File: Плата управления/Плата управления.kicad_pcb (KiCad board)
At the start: 6 copper layers, 67 x 68.5 mm, 114 parts, among them J1 Conn_02x10_Odd_Even, J10 Conn_02x03_Odd_Even, J2 CAN2, J3 CAN1, J4 A, J5 B, J6 C, J7 RS485, J8 Conn_02x03_Odd_Even, J9 Conn_01x06, U1 AT25xxx, U2 LMV7239M5, U3 LMV321, U4 STM32F767VITx, U5 INA283, U6 ADM3491ExR, U7 ASEMB-10

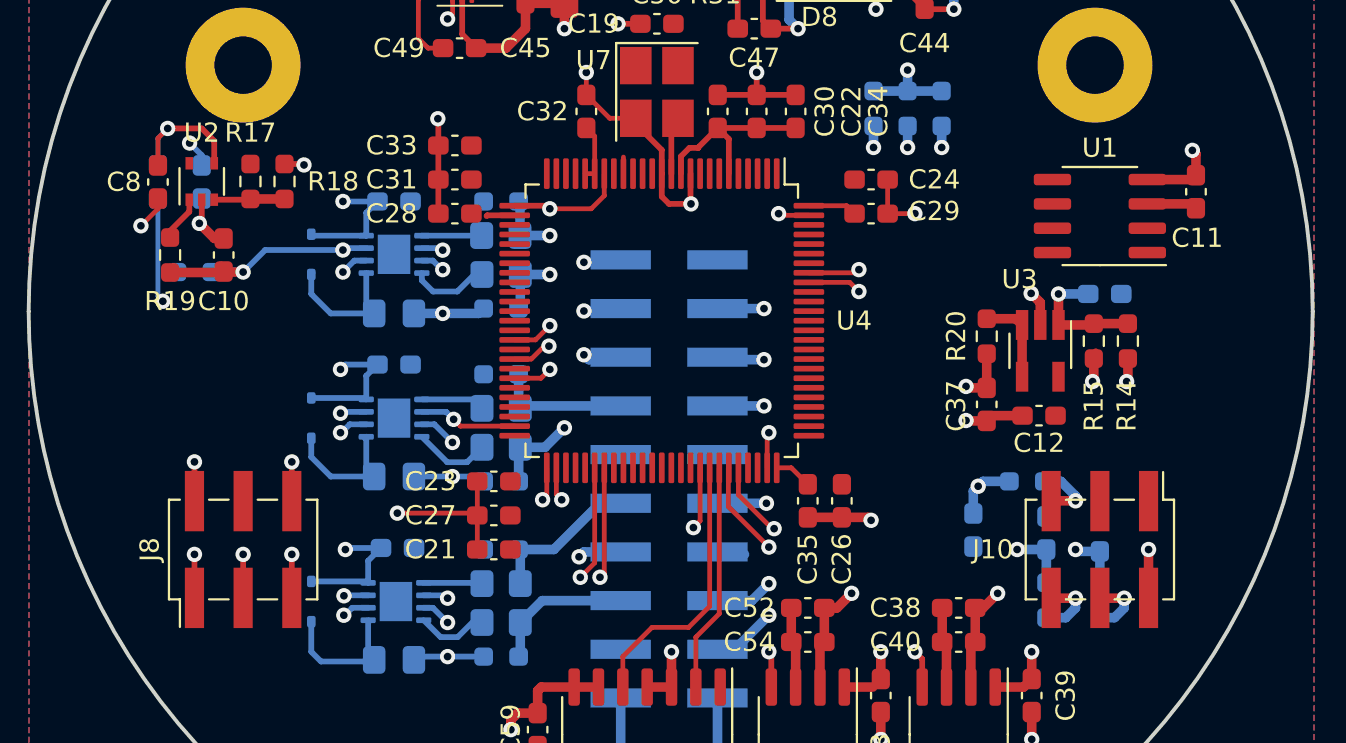
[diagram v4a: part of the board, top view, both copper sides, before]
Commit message: Изменил межплатный разъем
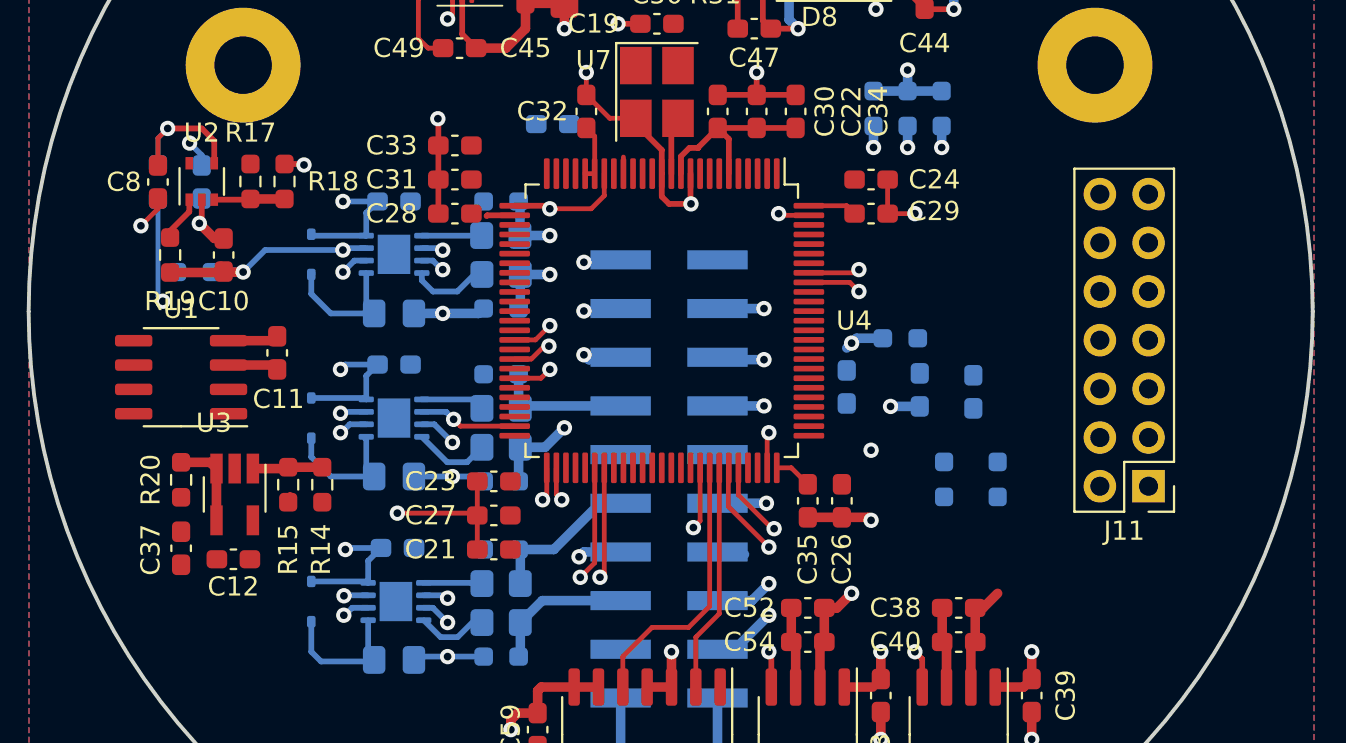
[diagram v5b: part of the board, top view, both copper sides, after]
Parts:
- removed J10, J8: Conn_02x03_Odd_Even, Connector_PinHeader_2.54mm:PinHeader_2x03_P2.54mm_Vertical_SMD
- added J11: Conn_02x07_Odd_Even, Connector_PinHeader_2.54mm:PinHeader_2x07_P2.54mm_Vertical, F.Cu at (108.2, 105.2)
- moved C11 48.7 mm to (62.7, 98.2)
- moved U1 48.7 mm to (57.7, 99.5)
- moved C37 42.7 mm to (57.7, 108.4)
- moved C12 42.7 mm to (60.5, 109.0)
- moved R15 42.7 mm to (63.3, 105.1)
- moved U3 42.7 mm to (60.5, 105.6)
- moved R20 42.7 mm to (57.7, 104.8)
- moved R14 42.7 mm to (65.1, 105.1)
- moved C36 30.1 mm to (77.1, 86.3)
- moved C20 9.97 mm to (96.3, 100.1)
- moved C60 9.97 mm to (99.1, 100.2)
- moved C61 9.97 mm to (92.5, 100.0)
- moved R41 9.97 mm to (95.2, 97.4)
- moved R39 8.26 mm to (97.5, 104.8)
- moved R40 8.26 mm to (100.3, 104.8)
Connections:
- U4 pad 89: unconnected-(U4-PB3-Pad89) -> SCK_MCU
- U4 pad 90: unconnected-(U4-PB4-Pad90) -> MISO_MCU
- U4 pad 91: unconnected-(U4-PB5-Pad91) -> MOSI_MCU
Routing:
- net GND: track 141.5 -> 129.4 mm, vias 34 -> 28
- net Temp_Coil2: track 3.52 -> 0.00 mm, vias 1 -> 0
- net Temp_Coil1: track 3.47 -> 0.00 mm, vias 1 -> 0
- net Temp_Coil3: track 3.26 -> 0.00 mm, vias 1 -> 0
- net Net-(U3-+): track 6.82 -> 3.65 mm, vias 1 -> 0
- net Temp_Coil3_MCU: track 2.94 -> 0.00 mm, vias 1 -> 0
- net DC_Voltage_MCU: track 2.89 -> 0.00 mm, vias 1 -> 0
- net SDIO_MCU: track 2.27 -> 0.00 mm, vias 1 -> 0
- net SCLK_MCU: track 2.27 -> 0.00 mm, vias 1 -> 0
- net CS_MCU: track 2.27 -> 0.00 mm, vias 1 -> 0
- net Current_A_MCU: track 2.05 -> 0.00 mm, vias 1 -> 0
- net Temp_Coil2_MCU: track 3.25 -> 1.52 mm
- net +24V: track 13.6 -> 12.4 mm, vias 3 -> 2
- net Temp_Coil1_MCU: track 3.26 -> 2.09 mm

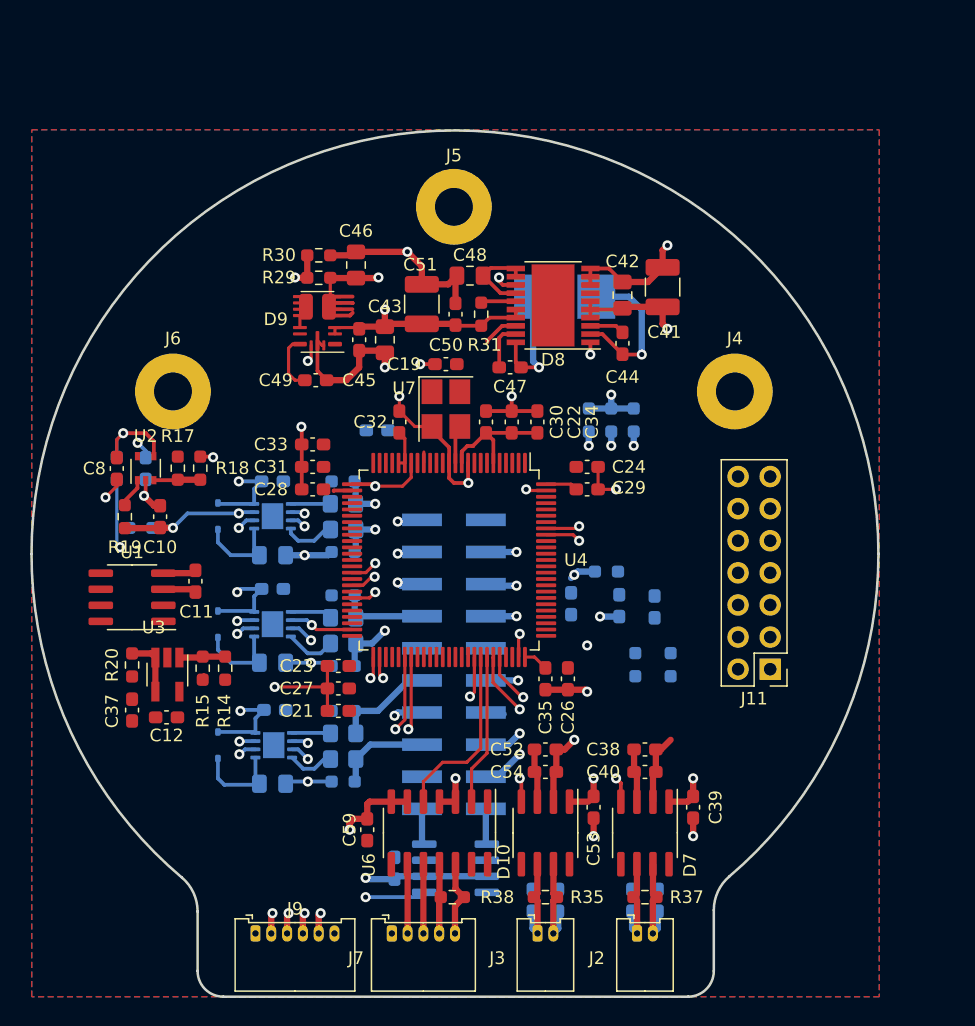
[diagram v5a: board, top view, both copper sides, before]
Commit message: Разделил аналоговое и цифровое питание
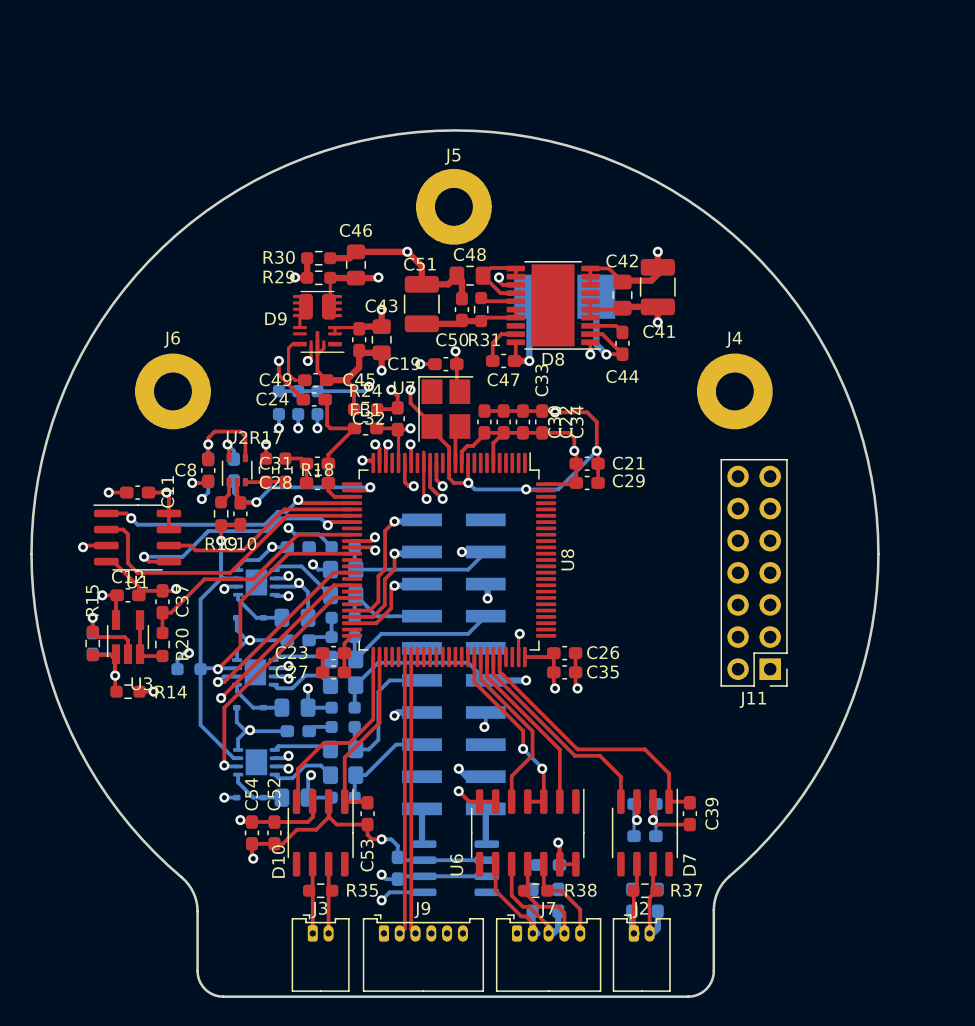
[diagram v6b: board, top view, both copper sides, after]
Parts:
- removed C20, C60, C61: 56p, Capacitor_SMD:C_0603_1608Metric_Pad1.08x0.95mm_HandSolder
- removed R39, R40, R41: 120, Resistor_SMD:R_0603_1608Metric_Pad0.98x0.95mm_HandSolder
- removed U4: STM32F767VITx, Package_QFP:LQFP-100_14x14mm_P0.5mm
- added FB1: BLM18KG102SH1D, Inductor_SMD:L_0603_1608Metric_Pad1.05x0.95mm_HandSolder, F.Cu at (76.2, 86.1)
- added R24: 0, Resistor_SMD:R_0603_1608Metric_Pad0.98x0.95mm_HandSolder, F.Cu at (76.2, 84.6)
- added U8: STM32F407VETx, Package_QFP:LQFP-100_14x14mm_P0.5mm, F.Cu at (82.8, 96.5)
- C38, C40, C59: moved to B.Cu
- J7: value RS485 -> RS-485
- moved C36 28.1 mm to (54.6, 103.1), turned to 90 degrees
- moved C21 27.7 mm to (93.7, 88.9), turned to 0 degrees
- moved R22 26.3 mm to (69.3, 84.1)
- moved R23 25.1 mm to (72.4, 84.1)
- moved C54 23.7 mm to (67.2, 118.1), turned to 90 degrees
- moved R21 23.0 mm to (70.9, 84.1)
- moved C52 22.4 mm to (69.0, 118.1), turned to 90 degrees
- moved C24 22.2 mm to (72.1, 83.8), turned to 180 degrees
- moved C33 18.2 mm to (90.2, 85.6), turned to 90 degrees
- moved C53 17.9 mm to (76.4, 116.6)
- moved R35 17.8 mm to (72.6, 122.7)
- moved D10 17.8 mm to (72.6, 118.1)
- moved J3 17.8 mm to (72.0, 126.1)
- moved D1 15.4 mm to (67.1, 108.2), turned to 180 degrees
- moved C59 14.6 mm to (90.7, 120.7), turned to 0 degrees
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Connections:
- C32 pad 1: VDDA -> +3.3VA
- C32 pad 2: GND -> GNDA
- J11 pad 10: Temp_Coil_A_MCU -> Current_C_MCU
- J11 pad 4: GNDA -> Temp_Coil_C_MCU
- J11 pad 6: Temp_Coil_C_MCU -> Temp_Coil_B_MCU
- J11 pad 8: Temp_Coil_B_MCU -> Temp_Coil_A_MCU
- J11 pad 9: Current_C_MCU -> GNDA
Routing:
- net GND: track 129.4 -> 175.0 mm
- net +3.3V: track 55.1 -> 96.4 mm, vias 4 -> 15
- net Temp_Coil_B_MCU: track 0.00 -> 37.7 mm, vias 0 -> 1
- net Temp_Coil_C_MCU: track 0.00 -> 37.6 mm, vias 0 -> 1
- net Temp_Coil_A_MCU: track 0.00 -> 35.7 mm, vias 0 -> 1
- net Analog_Input1: track 1.67 -> 36.4 mm
- net Analog_Input2: track 1.66 -> 35.3 mm
- net Current_B_MCU: track 0.00 -> 31.6 mm, vias 0 -> 1
- net Current_C_MCU: track 0.00 -> 30.2 mm, vias 0 -> 1
- net Current_A_MCU: track 0.00 -> 28.0 mm, vias 0 -> 1
- net MISO_MCU: track 0.00 -> 24.1 mm
- net ~{OS}_MCU: track 3.18 -> 24.8 mm
- net ~{CS_MCU}: track 0.00 -> 20.7 mm, vias 0 -> 2
- net MOSI_MCU: track 0.00 -> 20.3 mm, vias 0 -> 2
- net DC_Voltage_MCU: track 0.00 -> 19.2 mm
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- added copper zone on In4.Cu, net +3.3V
- added copper zone on In2.Cu, net +3.3VA
- added copper zone on In3.Cu, net GND
- added copper zone on In3.Cu, net GNDA
- removed copper zone on F.Cu, net +3.3V
- removed copper zone on In3.Cu, net +3.3V
- removed copper zone on In3.Cu, net Enable
- removed copper zone on B.Cu, net GND

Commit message: Редактировал схему
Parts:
- added R25: 1k, Resistor_SMD:R_0603_1608Metric_Pad0.98x0.95mm_HandSolder, F.Cu at (93.7, 93.5)
- added R26: 1k, Resistor_SMD:R_0603_1608Metric_Pad0.98x0.95mm_HandSolder, B.Cu at (80.5, 88.9)
- moved C55 17.8 mm to (73.7, 123.4)
- moved C56 17.8 mm to (71.6, 123.4)
- moved C5 1.78 mm to (69.1, 110.0)
- moved C1 1.78 mm to (69.1, 102.9)
- moved C3 1.78 mm to (69.1, 95.5)
- moved C57 0.25 mm to (99.1, 123.4)
- moved C58 0.25 mm to (97.0, 123.4)
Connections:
- net MISO_MCU renamed EEPROM_MISO_MCU
- net MOSI_MCU renamed EEPROM_MOSI_MCU
- net SCK_MCU renamed EEPROM_SCK_MCU
- net SCL_MCU renamed Temperature_Power_SCL_MCU
- net SDA_MCU renamed Temperature_Power_SDA_MCU
- net ~{CS_MCU} renamed EEPROM_~{CS_MCU}
- net ~{OS}_MCU renamed Temperature_Power_~{OS}_MCU
- C39 pad 2: CAN2_TXD_MCU -> CAN1_TXD_MCU
- C53 pad 2: CAN1_TXD_MCU -> CAN2_TXD_MCU
- C55 pad 2: CAN1H -> CAN2H
- C56 pad 1: CAN1L -> CAN2L
- C57 pad 2: CAN2H -> CAN1H
- C58 pad 1: CAN2L -> CAN1L
- D10 pad 1: CAN1_TXD_MCU -> CAN2_TXD_MCU
- D10 pad 4: CAN1_RXD_MCU -> CAN2_RXD_MCU
- D10 pad 6: CAN1L -> CAN2L
- D10 pad 7: CAN1H -> CAN2H
- D7 pad 1: CAN2_TXD_MCU -> CAN1_TXD_MCU
- D7 pad 4: CAN2_RXD_MCU -> CAN1_RXD_MCU
- D7 pad 6: CAN2L -> CAN1L
- D7 pad 7: CAN2H -> CAN1H
- D8 pad 7: unconnected-(D8-PS-Pad7) -> GND
- J11 pad 3: SCLK_MCU -> Angle_Sensor_CS_MCU
- J11 pad 5: CS_MCU -> Angle_Sensor_SCLK_MCU
- J11 pad 7: SDIO_MCU -> Angle_Sensor_SDIO_MCU
- J2 pad 1: CAN2L -> CAN1L
- J2 pad 2: CAN2H -> CAN1H
- J3 pad 1: CAN1L -> CAN2L
- J3 pad 2: CAN1H -> CAN2H
- R35 pad 1: CAN1L -> CAN2L
- R35 pad 2: CAN1H -> CAN2H
- R37 pad 1: CAN2L -> CAN1L
- R37 pad 2: CAN2H -> CAN1H
- U6 pad 2: RX_MCU -> RS_485_RX_MCU
- U6 pad 5: TX_MCU -> RS_485_TX_MCU
- U8 pad 14: unconnected-(U8-NRST-Pad14) -> NRST
- U8 pad 51: CAN1_RXD_MCU -> CAN2_RXD_MCU
- U8 pad 52: CAN1_TXD_MCU -> CAN2_TXD_MCU
- U8 pad 68: TX_MCU -> RS_485_RX_MCU
- U8 pad 69: RX_MCU -> RS_485_TX_MCU
- U8 pad 70: CAN2_RXD_MCU -> CAN1_RXD_MCU
- U8 pad 71: CAN2_TXD_MCU -> CAN1_TXD_MCU
- U8 pad 77: unconnected-(U8-PA15-Pad77) -> Angle_Sensor_CS_MCU
- U8 pad 78: unconnected-(U8-PC10-Pad78) -> Angle_Sensor_SCLK_MCU
- U8 pad 79: unconnected-(U8-PC11-Pad79) -> Angle_Sensor_SDIO_MCU
- U8 pad 94: unconnected-(U8-BOOT0-Pad94) -> BOOT0
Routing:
- net GND: track 175.0 -> 216.8 mm, vias 28 -> 34
- net +3.3V: track 96.4 -> 125.1 mm
- net Angle_Sensor_SDIO_MCU: track 0.00 -> 19.2 mm
- net Angle_Sensor_CS_MCU: track 0.00 -> 19.0 mm
- net Angle_Sensor_SCLK_MCU: track 0.00 -> 18.3 mm
- net RS_485_TX_MCU: track 0.00 -> 15.0 mm
- net RS_485_RX_MCU: track 0.00 -> 14.0 mm, vias 0 -> 2
- net RX_MCU: track 13.8 -> 0.00 mm
- net TX_MCU: track 13.8 -> 0.00 mm
- net CAN2_TXD_MCU: track 21.8 -> 14.4 mm
- net CAN1_TXD_MCU: track 14.4 -> 21.8 mm
- net NRST: track 0.00 -> 7.13 mm, vias 0 -> 1
- net BOOT0: track 0.00 -> 2.35 mm
- net CAN2_RXD_MCU: track 16.8 -> 15.6 mm
- net CAN1_RXD_MCU: track 15.6 -> 16.8 mm
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
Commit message: Ещё нужно доработать
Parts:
- removed C41: 10u, Capacitor_SMD:C_1210_3225Metric_Pad1.33x2.70mm_HandSolder
- removed C42: 470n, Capacitor_SMD:C_0805_2012Metric_Pad1.18x1.45mm_HandSolder
- removed C44, C47, C50: 100n, Capacitor_SMD:C_0603_1608Metric_Pad1.08x0.95mm_HandSolder
- removed C48: 4.7u, Capacitor_SMD:C_0805_2012Metric_Pad1.18x1.45mm_HandSolder
- removed C51: 22u, Capacitor_SMD:C_1210_3225Metric_Pad1.33x2.70mm_HandSolder
- removed D4, D6: ADP3110A, Package_DFN_QFN:DFN-8-1EP_3x3mm_P0.65mm_EP1.7x2.05mm
- removed D8: TPS55165QPWPRQ1, Package_SO:HTSSOP-20-1EP_4.4x6.5mm_P0.65mm_EP3.4x6.5mm
- removed L2: 4.7u, Inductor_my:LQH66SN100M03L
- removed R13: 10k, Resistor_SMD:R_0603_1608Metric_Pad0.98x0.95mm_HandSolder
- removed R31: 100k, Resistor_SMD:R_0603_1608Metric_Pad0.98x0.95mm_HandSolder
- added C13: 1u, Capacitor_SMD:C_0603_1608Metric_Pad1.08x0.95mm_HandSolder, B.Cu at (78.5, 85.1)
- added C14: 10u, Capacitor_SMD:C_0603_1608Metric_Pad1.08x0.95mm_HandSolder, B.Cu at (65.0, 113.8)
- added C15: BS, Capacitor_SMD:C_0805_2012Metric_Pad1.18x1.45mm_HandSolder, B.Cu at (66.0, 100.3)
- added C16: 100n, Capacitor_SMD:C_0603_1608Metric_Pad1.08x0.95mm_HandSolder, B.Cu at (77.0, 85.1)
- added C17: 1u, Capacitor_SMD:C_0603_1608Metric_Pad1.08x0.95mm_HandSolder, B.Cu at (75.4, 85.1)
- added C18: 10u, Capacitor_SMD:C_1210_3225Metric_Pad1.33x2.70mm_HandSolder, F.Cu at (94.0, 78.2)
- added C20: 10u, Capacitor_SMD:C_1210_3225Metric_Pad1.33x2.70mm_HandSolder, F.Cu at (94.0, 81.5)
- added C25: 10u, Capacitor_SMD:C_1210_3225Metric_Pad1.33x2.70mm_HandSolder, F.Cu at (88.9, 78.2)
- added L1: 33u, Inductor_SMD:L_10.4x10.4_H4.8, B.Cu at (92.5, 74.7)
- added R27: 2.7, Resistor_SMD:R_0805_2012Metric_Pad1.20x1.40mm_HandSolder, B.Cu at (74.7, 97.5)
- added R28: 10k, Resistor_SMD:R_0603_1608Metric_Pad0.98x0.95mm_HandSolder, B.Cu at (74.7, 101.3)
- added R32: 10k, Resistor_SMD:R_0603_1608Metric_Pad0.98x0.95mm_HandSolder, B.Cu at (74.7, 95.8)
- added U10: LM2594HVM-12, Package_SO:SOIC-8_3.9x4.9mm_P1.27mm, F.Cu at (91.2, 73.7)
- added U11: IR2184, Package_SO:SO-8_3.9x4.9mm_P1.27mm, B.Cu at (69.8, 108.0)
- added U4: IR2184, Package_SO:SO-8_3.9x4.9mm_P1.27mm, B.Cu at (69.8, 98.6)
- added U9: IR2184, Package_SO:SO-8_3.9x4.9mm_P1.27mm, B.Cu at (69.8, 116.3)
- C5: value 10u -> 2.2u; moved to F.Cu
- C6: value BS -> 2.2u; footprint Capacitor_SMD:C_0805_2012Metric_Pad1.18x1.45mm_HandSolder -> Capacitor_SMD:C_0603_1608Metric_Pad1.08x0.95mm_HandSolder; moved to F.Cu
- D2: value ADP3110A -> D_Small; footprint Package_DFN_QFN:DFN-8-1EP_3x3mm_P0.65mm_EP1.7x2.05mm -> Diode_SMD:D_SOD-323
- D5: value D_Small -> MBRA320; footprint Diode_SMD:D_SOD-323 -> Diode_SMD:D_SMA; moved to F.Cu
- R1: value 10k -> 2.7; footprint Resistor_SMD:R_0603_1608Metric_Pad0.98x0.95mm_HandSolder -> Resistor_SMD:R_0805_2012Metric_Pad1.20x1.40mm_HandSolder
- R10, R11: value 2.7 -> 0; footprint Resistor_SMD:R_0805_2012Metric_Pad1.20x1.40mm_HandSolder -> Resistor_SMD:R_0603_1608Metric_Pad0.98x0.95mm_HandSolder; moved to F.Cu
- R12: value 10k -> 0; moved to F.Cu
- R14: value 10k -> 9.1k
- R15: value 10k -> 1k
- moved D5 51.9 mm to (97.0, 72.9), turned to -90 degrees
- moved R10 27.7 mm to (81.8, 86.9), turned to 180 degrees
- moved R12 26.0 mm to (94.7, 99.1)
- moved R8 23.6 mm to (74.7, 119.1)
- moved R11 23.1 mm to (94.7, 100.6)
- moved C5 23.0 mm to (91.9, 108.0), turned to 0 degrees
- moved R6 20.1 mm to (74.7, 117.3)
- moved C4 17.6 mm to (66.0, 118.1), turned to 90 degrees
- moved D3 17.3 mm to (64.0, 118.1), turned to 90 degrees
- moved R7 16.0 mm to (74.7, 115.3)
- moved R1 13.6 mm to (74.7, 99.6)
- moved R9 12.4 mm to (74.7, 113.5)
- moved C3 10.7 mm to (65.0, 105.4), turned to 0 degrees
- moved C6 10.6 mm to (71.1, 104.7), turned to -90 degrees
- moved C1 7.96 mm to (65.0, 96.0)
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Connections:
- C2 pad 1: A -> Net-(D1-K)
- C2 pad 2: Net-(D1-K) -> A
- C3 pad 1: GND -> +12V
- C3 pad 2: +12V -> GND
- C4 pad 1: B -> Net-(D3-K)
- C4 pad 2: Net-(D3-K) -> C
- C5 pad 1: GND -> Net-(U8-VCAP_2)
- C5 pad 2: +12V -> GND
- C6 pad 1: C -> Net-(U8-VCAP_1)
- C6 pad 2: Net-(D5-K) -> GND
- C8 pad 1: Net-(U2--) -> Net-(U2-+)
- D2 pad 1: Net-(D1-K) -> Net-(D2-K)
- D2 pad 2: IN_A -> +12V
- D5 pad 2: +12V -> GND
- J11 pad 9: GNDA -> OUT_MCU
- R1 pad 1: GND -> Net-(U4-HO)
- R1 pad 2: Enable -> G3
- R10 pad 1: Net-(D6-DRVH) -> Net-(U8-PH1)
- R10 pad 2: G5 -> GND
- R11 pad 1: Net-(D6-DRVL) -> Net-(U8-PC11)
- R11 pad 2: G6 -> Angle_Sensor_SDIO_MCU
- R12 pad 1: C -> Net-(U8-PC12)
- R12 pad 2: G5 -> Angle_Sensor_SDIO_MCU
- R16 pad 1: Net-(U2--) -> Net-(U2-+)
- R17 pad 2: Net-(U2-+) -> Net-(U2--)
- R18 pad 1: Net-(U2-+) -> Net-(U2--)
- R2 pad 1: Net-(D2-DRVH) -> Net-(U11-HO)
- R3 pad 1: Net-(D2-DRVL) -> Net-(U11-LO)
- R6 pad 2: G3 -> G5
- R7 pad 2: G4 -> G6
- R8 pad 1: B -> C
- R8 pad 2: G3 -> G5
- R9 pad 2: G4 -> G6
- U8 pad 13: GND -> Net-(U8-PH1)
- U8 pad 33: unconnected-(U8-PC4-Pad33) -> OUT_MCU
- U8 pad 49: unconnected-(U8-VCAP_1-Pad49) -> Net-(U8-VCAP_1)
- U8 pad 73: unconnected-(U8-VCAP_2-Pad73) -> Net-(U8-VCAP_2)
- U8 pad 79: Angle_Sensor_SDIO_MCU -> Net-(U8-PC11)
- U8 pad 80: unconnected-(U8-PC12-Pad80) -> Net-(U8-PC12)
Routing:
- net GND: track 216.8 -> 273.3 mm, vias 34 -> 28
- net OUT_MCU: track 0.00 -> 39.2 mm, vias 0 -> 3
- net C: track 17.7 -> 40.2 mm
- net +12V: track 35.2 -> 56.1 mm, vias 5 -> 7
- net IN_B: track 24.4 -> 8.45 mm, vias 2 -> 1
- net Net-(D8-L1): track 9.38 -> 0.00 mm, vias 1 -> 0
- net A: track 22.9 -> 31.4 mm
- net Net-(D8-L2): track 7.89 -> 0.00 mm, vias 1 -> 0
- net Net-(D8-VOS_FB): track 6.67 -> 0.00 mm
- net Net-(D5-K): track 4.58 -> 11.2 mm, vias 0 -> 1
- net Net-(U8-VCAP_1): track 0.00 -> 6.15 mm
- net Net-(U11-HO): track 0.00 -> 6.07 mm
- net Net-(U8-VCAP_2): track 0.00 -> 5.95 mm
- net Enable: track 45.9 -> 51.8 mm, vias 2 -> 4
- net Net-(U4-HO): track 0.00 -> 5.65 mm
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- added copper zone on F.Cu, net +12V
- added copper zone on F.Cu, net +24V
- added copper zone on F.Cu, net GND
